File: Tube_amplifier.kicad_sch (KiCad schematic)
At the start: 31 parts, among them J1 AudioJack3, T1 Transformer_SP_1S, U1 6N2P, U2 6P14P, U3 6H2P

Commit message: Amplifier ready
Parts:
- added C12, C13: 10uF, spdf1626_lib:C_THT_D10.0mm_P5.00mm, symbol Device:C
- added J2: Input, spdf1626_lib:PinHeader_1x02_P2.54mm, symbol Connector_Generic:Conn_01x02
- added J3: Conn_01x04, spdf1626_lib:PinHeader_1x04_P2.54mm, symbol Connector_Generic:Conn_01x04
- added J4: output, spdf1626_lib:PinHeader_1x02_P2.54mm, symbol Connector_Generic:Conn_01x02
- RV1: footprint (none) -> spdf1626_lib:PinHeader_1x03_P2.54mm
- RV2, RV3: footprint (none) -> spdf1626_lib:Potentiometer_THT_CA9V
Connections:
- net +6V: now also J3.2 (Pin_2)
- net 240V: now also C12.1, C13.1, J3.4 (Pin_4)
- net GND: now also R11.2, T1.5 (S2), C12.2, C13.2, J2.2 (Pin_2), J3.1 (Pin_1), J3.3 (Pin_3), J4.2 (Pin_2); no longer R11.1, T1.4 (S1)
- net Left_output: now also T1.4 (S1), J4.1 (Pin_1); no longer T1.5 (S2)
- net at C11.2, R1.1: now also R11.1; no longer R11.2
- net at R4.1: now also RV2.1; no longer RV2.3
- net at C5.2, R5.2: now also RV2.3; no longer RV2.1
- net Left_input: no longer names the net of C2.1
- net Left_input: now also J2.1 (Pin_1)
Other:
- moved on the sheet: R11, T1

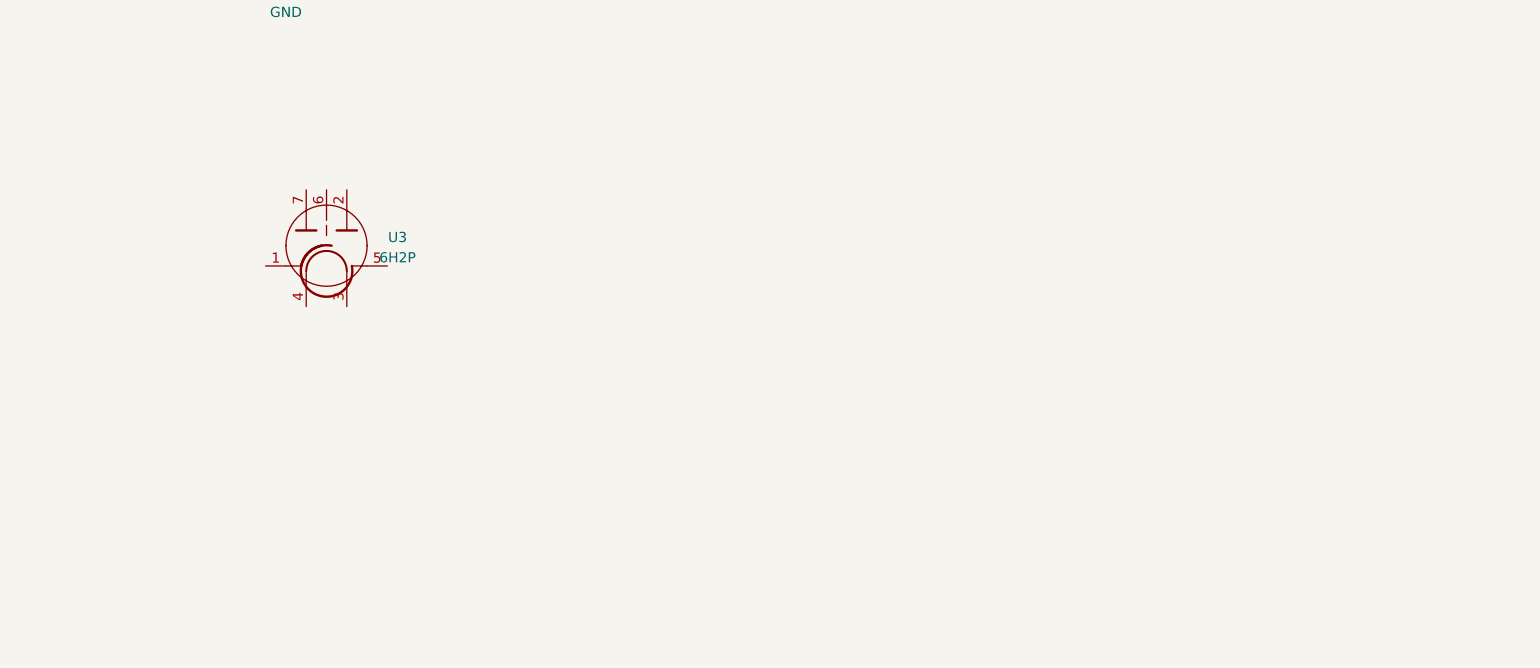
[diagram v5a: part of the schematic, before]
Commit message: Power supply added
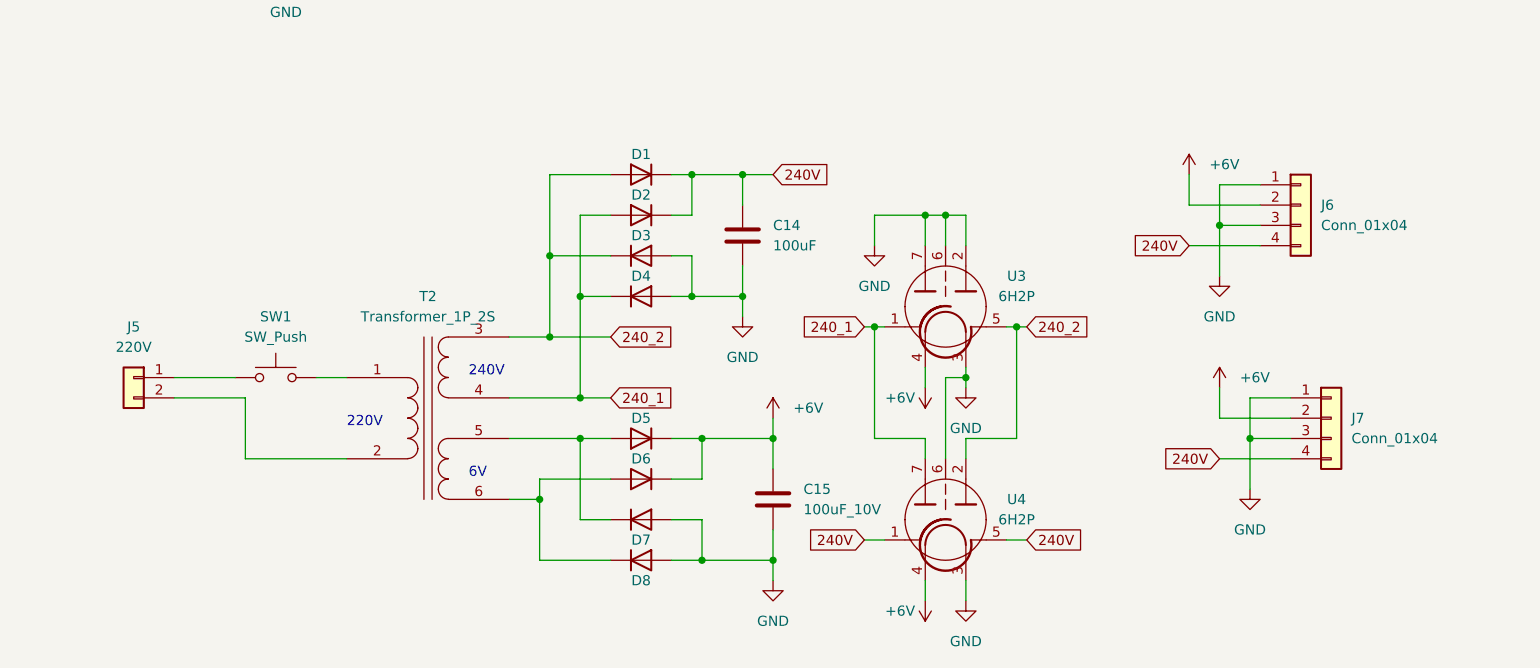
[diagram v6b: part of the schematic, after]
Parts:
- added C14: 100uF, Capacitor_THT:CP_Radial_D22.0mm_P10.00mm_SnapIn, symbol Device:C
- added C15: 100uF_10V, Capacitor_THT:CP_Radial_D6.3mm_P2.50mm, symbol Device:C
- added D1, D2, D3, D4: 1n4007, Diode_THT:D_DO-41_SOD81_P12.70mm_Horizontal, symbol Device:D
- added D5, D6, D7, D8: 10A10, Diode_THT:D_DO-27_P15.24mm_Horizontal, symbol Device:D
- added J5: 220V, Connector_Phoenix_MC_HighVoltage:PhoenixContact_MCV_1,5_2-G-5.08_1x02_P5.08mm_Vertical, symbol Connector_Generic:Conn_01x02
- added J6, J7: Conn_01x04, spdf1626_lib:PinHeader_1x04_P2.54mm, symbol Connector_Generic:Conn_01x04
- added SW1: SW_Push, spdf1626_lib:PinHeader_1x02_P2.54mm, symbol Switch:SW_Push
- added T2: Transformer_1P_2S, symbol Device:Transformer_1P_2S
- added U4: 6H2P, spdf1626_lib:7-pin_tube_socket, symbol spdf1626:6H2P
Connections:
- net +6V: now also U3.4, C15.1, D5.1 (K), D6.1 (K), J6.2 (Pin_2), J7.2 (Pin_2), U4.4
- net 240V: now also C14.1, D1.1 (K), D2.1 (K), J6.4 (Pin_4), J7.4 (Pin_4), U4.1, U4.5
- net GND: now also U3.2, U3.3, U3.6, U3.7, C14.2, C15.2, D3.2 (A), D4.2 (A), D7.2 (A), D8.2 (A), J6.1 (Pin_1), J6.3 (Pin_3), J7.1 (Pin_1), J7.3 (Pin_3), U4.3, U4.6
- net 240_1: now reaches U3.1
- net 240_1: now also D2.2 (A), D4.1 (K), T2.4 (SB), U4.7
- net 240_2: now reaches U3.5
- net 240_2: now also D1.2 (A), D3.1 (K), T2.3 (SA), U4.2
- new net: D6.2 (A), D8.1 (K), T2.6 (SD)
- new net: D5.2 (A), D7.1 (K), T2.5 (SC)
- new net: J5.1 (Pin_1), SW1.1
- new net: J5.2 (Pin_2), T2.2 (AB)
- new net: SW1.2, T2.1 (AA)
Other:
- note added: "220V"
- note added: "240V"
- note added: "6V"
- moved on the sheet: U3

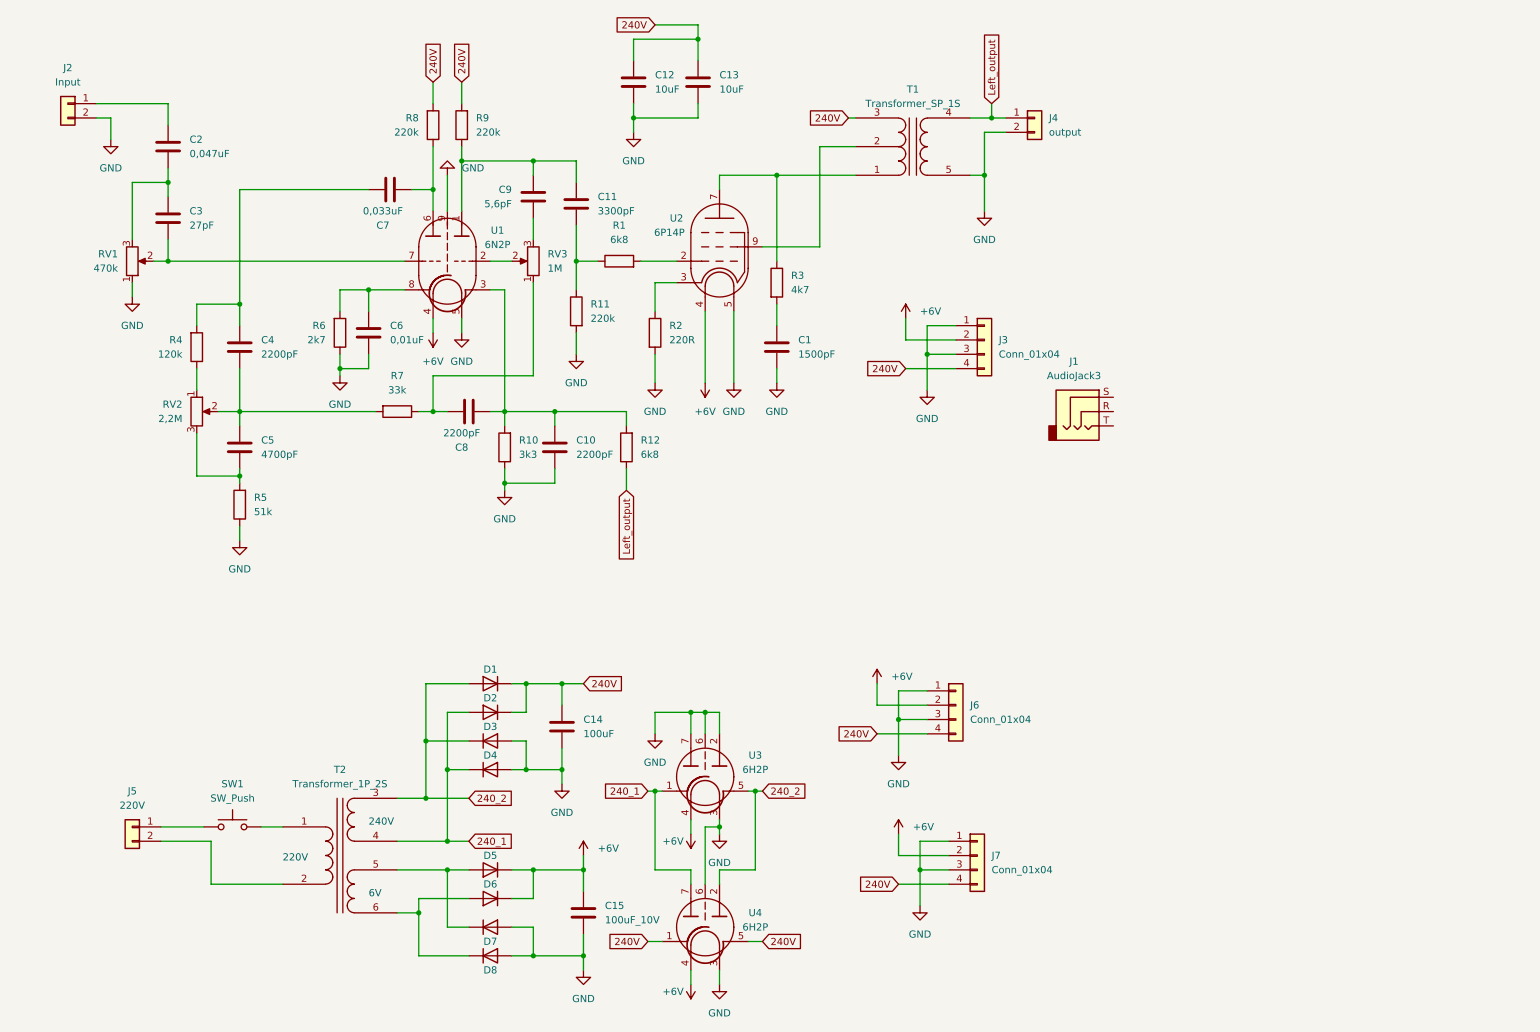
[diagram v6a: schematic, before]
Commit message: Indication board completed
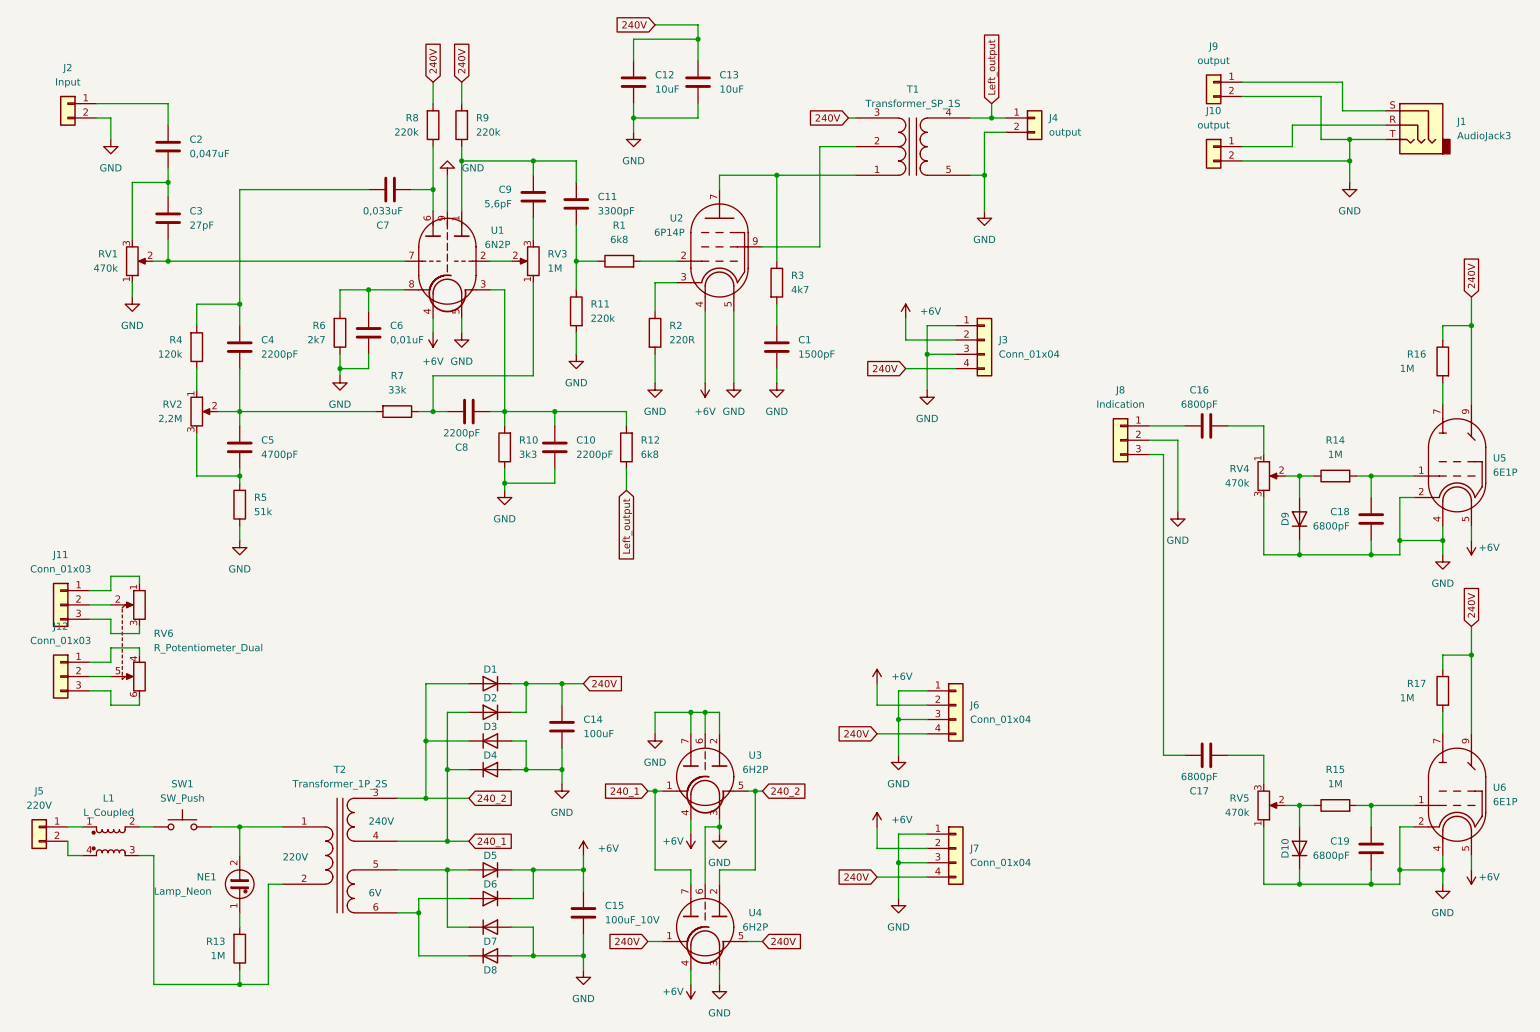
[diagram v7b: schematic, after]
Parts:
- added C16, C17, C18, C19: 6800pF, spdf1626_lib:C_THT_K73-17_P5.00mm, symbol Device:C
- added D10, D9: 1n4007, Diode_THT:D_DO-41_SOD81_P12.70mm_Horizontal, symbol Device:D
- added J10, J9: output, spdf1626_lib:PinHeader_1x02_P2.54mm, symbol Connector_Generic:Conn_01x02
- added J11, J12: Conn_01x03, spdf1626_lib:PinHeader_1x03_P2.54mm, symbol Connector_Generic:Conn_01x03
- added J8: Indication, spdf1626_lib:PinHeader_1x03_P2.54mm, symbol Connector_Generic:Conn_01x03
- added L1: L_Coupled, spdf1626_lib:L_THT_PLA10, symbol spdf1626:L_Coupled
- added NE1: Lamp_Neon, spdf1626_lib:PinHeader_1x02_P2.54mm, symbol Device:Lamp_Neon
- added R13, R14, R15, R16, R17: 1M, spdf1626_lib:R_THT_025W, symbol Device:R
- added RV4, RV5: 470k, spdf1626_lib:Potentiometer_THT_CA9V, symbol Device:R_Potentiometer
- added RV6: R_Potentiometer_Dual, Potentiometer_THT:Potentiometer_Alps_RK163_Dual_Horizontal, symbol Device:R_Potentiometer_Dual
- added U5, U6: 6E1P, spdf1626_lib:9-pin_tube_socket, symbol spdf1626:6E1P
- J1: footprint (none) -> Connector_Audio:Jack_6.35mm_Neutrik_NMJ6HHD2_Horizontal
- SW1: footprint spdf1626_lib:PinHeader_1x02_P2.54mm -> Button_Switch_THT:SW_Push_1P2T_Vertical_E-Switch_800UDP8P1A1M6
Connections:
- net +6V: now also U5.5, U6.5
- net 240V: now also R16.1, R17.1, U5.9, U6.9
- net GND: now also J1.T, C18.2, C19.2, D10.1 (K), D9.1 (K), J10.2 (Pin_2), J8.2 (Pin_2), J9.2 (Pin_2), RV4.3, RV5.1, U5.2, U5.4, U6.2, U6.4
- net at J5.1 (Pin_1): now also L1.1; no longer SW1.1
- net at J5.2 (Pin_2): now also L1.4; no longer T2.2 (AB)
- net at SW1.2: now also L1.2; no longer T2.1 (AA)
- net at J1.R: now also J10.1 (Pin_1)
- net at J1.S: now also J9.1 (Pin_1)
- new net: C19.1, R15.2, U6.1
- new net: R17.2, U6.7
- new net: D10.2 (A), R15.1, RV5.2
- new net: L1.3, R13.1, T2.2 (AB)
- new net: D9.2 (A), R14.1, RV4.2
- new net: C18.1, R14.2, U5.1
- new net: R16.2, U5.7
- new net: NE1.1, R13.2
- new net: NE1.2, SW1.1, T2.1 (AA)
- new net: C16.1, J8.1 (Pin_1)
- new net: C16.2, RV4.1
- new net: J11.1 (Pin_1), RV6.1
- new net: J11.2 (Pin_2), RV6.2
- new net: J11.3 (Pin_3), RV6.3
- new net: C17.1, J8.3 (Pin_3)
- new net: J12.1 (Pin_1), RV6.4
- new net: J12.2 (Pin_2), RV6.5
- new net: J12.3 (Pin_3), RV6.6
- new net: C17.2, RV5.3
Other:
- moved on the sheet: J1, J5, J7, SW1

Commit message: Some cleaning
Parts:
- added J13: Conn_01x04, spdf1626_lib:PinHeader_1x04_P2.54mm, symbol Connector_Generic:Conn_01x04
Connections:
- net +6V: now also J13.2 (Pin_2)
- net 240V: now also J13.4 (Pin_4)
- net GND: now also J13.1 (Pin_1), J13.3 (Pin_3)
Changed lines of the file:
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@@
   (junction (at 111.76 130.81) (diameter 0) (color 0 0 0 0)
   )
+  (junction (at 171.45 113.03) (diameter 0) (color 0 0 0 0)
+  )
   (junction (at 139.7 156.21) (diameter 0) (color 0 0 0 0)
   )
@@
     (stroke (width 0) (type default) (color 0 0 0 0))
   )
+  (wire (pts (xy 171.45 113.03) (xy 176.53 113.03))
+    (stroke (width 0) (type default) (color 0 0 0 0))
+  )
   (wire (pts (xy 128.27 139.7) (xy 128.27 135.89))
     (stroke (width 0) (type default) (color 0 0 0 0))
@@
     (stroke (width 0) (type default) (color 0 0 0 0))
   )
+  (wire (pts (xy 167.64 110.49) (xy 167.64 106.68))
+    (stroke (width 0) (type default) (color 0 0 0 0))
+  )
   (wire (pts (xy 59.69 184.15) (xy 54.61 184.15))
     (stroke (width 0) (type default) (color 0 0 0 0))
@@
     (stroke (width 0) (type default) (color 0 0 0 0))
   )
+  (wire (pts (xy 171.45 113.03) (xy 171.45 107.95))
+    (stroke (width 0) (type default) (color 0 0 0 0))
+  )
   (wire (pts (xy 88.9 35.56) (xy 88.9 43.18))
     (stroke (width 0) (type default) (color 0 0 0 0))
@@
     (stroke (width 0) (type default) (color 0 0 0 0))
   )
+  (wire (pts (xy 171.45 119.38) (xy 171.45 113.03))
+    (stroke (width 0) (type default) (color 0 0 0 0))
+  )
   (wire (pts (xy 167.64 165.1) (xy 176.53 165.1))
     (stroke (width 0) (type default) (color 0 0 0 0))
@@
     (stroke (width 0) (type default) (color 0 0 0 0))
   )
+  (wire (pts (xy 171.45 107.95) (xy 176.53 107.95))
+    (stroke (width 0) (type default) (color 0 0 0 0))
+  )
   (wire (pts (xy 135.89 27.94) (xy 135.89 30.48))
     (stroke (width 0) (type default) (color 0 0 0 0))
@@
     (stroke (width 0) (type default) (color 0 0 0 0))
   )
+  (wire (pts (xy 167.64 115.57) (xy 176.53 115.57))
+    (stroke (width 0) (type default) (color 0 0 0 0))
+  )
   (wire (pts (xy 95.25 173.99) (xy 91.44 173.99))
     (stroke (width 0) (type default) (color 0 0 0 0))
@@
     (stroke (width 0) (type default) (color 0 0 0 0))
   )
+  (wire (pts (xy 176.53 110.49) (xy 167.64 110.49))
+    (stroke (width 0) (type default) (color 0 0 0 0))
+  )
   (wire (pts (xy 128.27 163.83) (xy 128.27 149.86))
     (stroke (width 0) (type default) (color 0 0 0 0))
@@
     )
   )
+  (global_label "240V" (shape input) (at 167.64 115.57 180) (fields_autoplaced)
+    (effects (font (size 1.27 1.27)) (justify right))
+    (property "Обозначения листов" "${INTERSHEET_REFS}" (id 0) (at 160.5098 115.6494 0)
+      (effects (font (size 1.27 1.27)) (justify right) hide)
+    )
+  )
   (global_label "240_2" (shape input) (at 95.25 151.13 0) (fields_autoplaced)
     (effects (font (size 1.27 1.27)) (justify left))
@@
     (pin "1")
   )
+  (symbol (lib_id "power:GND") (at 171.45 119.38 0) (unit 1)
+    (in_bom yes) (on_board yes) (fields_autoplaced)
+    (property "Reference" "#PWR034" (id 0) (at 171.45 125.73 0)
+      (effects (font (size 1.27 1.27)) hide)
+    )
+    (property "Value" "GND" (id 1) (at 171.45 124.46 0))
+    (property "Footprint" "" (id 2) (at 171.45 119.38 0)
+      (effects (font (size 1.27 1.27)) hide)
+    )
+    (property "Datasheet" "" (id 3) (at 171.45 119.38 0)
+      (effects (font (size 1.27 1.27)) hide)
+    )
+    (pin "1")
+  )
   (symbol (lib_id "Device:C") (at 111.76 138.43 0) (unit 1)
     (in_bom yes) (on_board yes) (fields_autoplaced)
@@
     (pin "2")
   )
+  (symbol (lib_id "power:+6V") (at 167.64 106.68 0) (unit 1)
+    (in_bom yes) (on_board yes) (fields_autoplaced)
+    (property "Reference" "#PWR033" (id 0) (at 167.64 110.49 0)
+      (effects (font (size 1.27 1.27)) hide)
+    )
+    (property "Value" "+6V" (id 1) (at 170.18 105.4099 0)
+      (effects (font (size 1.27 1.27)) (justify left))
+    )
+    (property "Footprint" "" (id 2) (at 167.64 106.68 0)
+      (effects (font (size 1.27 1.27)) hide)
+    )
+    (property "Datasheet" "" (id 3) (at 167.64 106.68 0)
+      (effects (font (size 1.27 1.27)) hide)
+    )
+    (pin "1")
+  )
   (symbol (lib_id "power:+6V") (at 134.62 157.48 0) (mirror x) (unit 1)
     (in_bom yes) (on_board yes)
@@
     (pin "2")
   )
+  (symbol (lib_id "Connector_Generic:Conn_01x04") (at 181.61 110.49 0) (unit 1)
+    (in_bom yes) (on_board yes) (fields_autoplaced)
+    (property "Reference" "J13" (id 0) (at 184.15 110.4899 0)
+      (effects (font (size 1.27 1.27)) (justify left))
+    )
+    (property "Value" "Conn_01x04" (id 1) (at 184.15 113.0299 0)
+      (effects (font (size 1.27 1.27)) (justify left))
+    )
+    (property "Footprint" "spdf1626_lib:PinHeader_1x04_P2.54mm" (id 2) (at 181.61 110.49 0)
+      (effects (font (size 1.27 1.27)) hide)
+    )
+    (property "Datasheet" "~" (id 3) (at 181.61 110.49 0)
+      (effects (font (size 1.27 1.27)) hide)
+    )
+    (pin "1")
+    (pin "2")
+    (pin "3")
+    (pin "4")
+  )
   (symbol (lib_id "spdf1626:6P14P") (at 139.7 54.61 0) (unit 1)
     (in_bom yes) (on_board yes)
@@
       (reference "#PWR032") (unit 1) (value "GND") (footprint "")
     )
+    (path "/a08b0e5e-2d13-4139-b701-15274c61f55e"
+      (reference "#PWR033") (unit 1) (value "+6V") (footprint "")
+    )
+    (path "/18662ccf-1e33-467c-ab2c-5d836cd17a53"
+      (reference "#PWR034") (unit 1) (value "GND") (footprint "")
+    )
     (path "/174e99dc-92b2-4f3c-b711-6020058d5916"
       (reference "#PWR0101") (unit 1) (value "GND") (footprint "")
@@
       (reference "J12") (unit 1) (value "Conn_01x03") (footprint "spdf1626_lib:PinHeader_1x03_P2.54mm")
     )
+    (path "/e1b76c94-0f39-4c85-90a0-15d04db4a572"
+      (reference "J13") (unit 1) (value "Conn_01x04") (footprint "spdf1626_lib:PinHeader_1x04_P2.54mm")
+    )
     (path "/374b0000-4530-46d2-ae7c-9589b2c363f1"
